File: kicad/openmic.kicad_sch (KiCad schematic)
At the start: 0 parts

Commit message: #13
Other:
- sheet codec ports: added CCLK; removed none
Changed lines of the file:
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@@
+	(wire
+		(pts
+			(xy 157.48 132.08) (xy 146.05 132.08)
+		)
+		(stroke
+			(width 0)
+			(type default)
+		)
+	)
 	(wire
 		(pts
@@
 	(wire
 		(pts
-			(xy 161.29 95.25) (xy 161.29 132.08)
-		)
-		(stroke
-			(width 0)
-			(type default)
-		)
-	)
-	(wire
-		(pts
-			(xy 146.05 132.08) (xy 161.29 132.08)
+			(xy 161.29 95.25) (xy 161.29 135.89)
+		)
+		(stroke
+			(width 0)
+			(type default)
+		)
+	)
+	(wire
+		(pts
+			(xy 146.05 135.89) (xy 161.29 135.89)
 		)
 		(stroke
@@
 	(wire
 		(pts
+			(xy 157.48 99.06) (xy 157.48 132.08)
+		)
+		(stroke
+			(width 0)
+			(type default)
+		)
+	)
+	(wire
+		(pts
 			(xy 101.6 139.7) (xy 101.6 91.44)
 		)
@@
 	(wire
 		(pts
+			(xy 146.05 99.06) (xy 157.48 99.06)
+		)
+		(stroke
+			(width 0)
+			(type default)
+		)
+	)
+	(wire
+		(pts
 			(xy 146.05 106.68) (xy 149.86 106.68)
 		)
@@
 	(wire
 		(pts
-			(xy 165.1 91.44) (xy 165.1 135.89)
+			(xy 165.1 91.44) (xy 165.1 139.7)
 		)
 		(stroke
@@
 	(wire
 		(pts
-			(xy 146.05 135.89) (xy 165.1 135.89)
+			(xy 146.05 139.7) (xy 165.1 139.7)
 		)
 		(stroke
@@
 		)
 		(pin "DIN" input
+			(at 146.05 139.7 0)
+			(effects
+				(font
+					(size 1.27 1.27)
+				)
+				(justify right)
+			)
+		)
+		(pin "DOUT" output
 			(at 146.05 135.89 0)
-			(effects
-				(font
-					(size 1.27 1.27)
-				)
-				(justify right)
-			)
-		)
-		(pin "DOUT" output
-			(at 146.05 132.08 0)
 			(effects
 				(font
@@
 			(effects
 				(font
+					(size 1.27 1.27)
+				)
+				(justify right)
+			)
+		)
+		(pin "CCLK" input
+			(at 146.05 132.08 0)
+			(effects
+				(font

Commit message: #14
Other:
- sheet input ports: added LED_1_DIN, LED_1_DOUT, LED_2_DIN, LED_2_DOUT; removed none
- sheet usb bridge ports: added LED_CONTROL; removed none
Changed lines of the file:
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@@
+	(wire
+		(pts
+			(xy 53.34 48.26) (xy 120.65 48.26)
+		)
+		(stroke
+			(width 0)
+			(type default)
+		)
+	)
 	(wire
 		(pts
@@
 	(wire
 		(pts
+			(xy 57.15 57.15) (xy 53.34 57.15)
+		)
+		(stroke
+			(width 0)
+			(type default)
+		)
+	)
+	(wire
+		(pts
 			(xy 120.65 132.08) (xy 109.22 132.08)
 		)
@@
 	(wire
 		(pts
-			(xy 53.34 30.48) (xy 53.34 54.61)
+			(xy 49.53 38.1) (xy 49.53 80.01)
 		)
 		(stroke
@@
 	(wire
 		(pts
-			(xy 53.34 30.48) (xy 57.15 30.48)
+			(xy 49.53 38.1) (xy 57.15 38.1)
 		)
 		(stroke
@@
 	(wire
 		(pts
+			(xy 53.34 64.77) (xy 57.15 64.77)
+		)
+		(stroke
+			(width 0)
+			(type default)
+		)
+	)
+	(wire
+		(pts
 			(xy 113.03 87.63) (xy 120.65 87.63)
 		)
@@
 	(wire
 		(pts
+			(xy 53.34 48.26) (xy 53.34 57.15)
+		)
+		(stroke
+			(width 0)
+			(type default)
+		)
+	)
+	(wire
+		(pts
 			(xy 153.67 128.27) (xy 153.67 102.87)
 		)
@@
 	(wire
 		(pts
-			(xy 57.15 54.61) (xy 53.34 54.61)
+			(xy 57.15 80.01) (xy 49.53 80.01)
 		)
 		(stroke
@@
 	(wire
 		(pts
+			(xy 57.15 60.96) (xy 53.34 60.96)
+		)
+		(stroke
+			(width 0)
+			(type default)
+		)
+	)
+	(wire
+		(pts
 			(xy 82.55 95.25) (xy 97.79 95.25)
+		)
+		(stroke
+			(width 0)
+			(type default)
+		)
+	)
+	(wire
+		(pts
+			(xy 53.34 60.96) (xy 53.34 64.77)
 		)
 		(stroke
@@
 		)
 		(pin "+48V_PH" input
-			(at 57.15 54.61 180)
+			(at 57.15 80.01 180)
 			(effects
 				(font
@@
 		)
 		(pin "BSY_1" output
-			(at 57.15 59.69 180)
+			(at 57.15 72.39 180)
 			(effects
 				(font
@@
 		)
 		(pin "BSY_2" output
-			(at 57.15 63.5 180)
+			(at 57.15 76.2 180)
 			(effects
 				(font
@@
 				)
 				(justify right)
+			)
+		)
+		(pin "LED_1_DIN" input
+			(at 57.15 57.15 180)
+			(effects
+				(font
+					(size 1.27 1.27)
+				)
+				(justify left)
+			)
+		)
+		(pin "LED_1_DOUT" output
+			(at 57.15 60.96 180)
+			(effects
+				(font
+					(size 1.27 1.27)
+				)
+				(justify left)
+			)
+		)
+		(pin "LED_2_DIN" input
+			(at 57.15 64.77 180)
+			(effects
+				(font
+					(size 1.27 1.27)
+				)
+				(justify left)
+			)
+		)
+		(pin "LED_2_DOUT" output
+			(at 57.15 68.58 180)
+			(effects
+				(font
+					(size 1.27 1.27)
+				)
+				(justify left)
 			)
 		)
@@
 		)
 		(pin "+48V_PH" output
-			(at 57.15 30.48 180)
+			(at 57.15 38.1 180)
 			(effects
 				(font
@@
 			(effects
 				(font
+					(size 1.27 1.27)
+				)
+				(justify left)
+			)
+		)
+		(pin "LED_CONTROL" output
+			(at 120.65 48.26 180)
+			(effects
+				(font

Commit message: phones out
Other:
- added sheet monitor (monitor.kicad_sch)
- sheet heaphone driver ports: added LED_DIN, LED_DOUT, PHONES_EN, PHONES_IND, ROT_A, ROT_B; removed none
- sheet line driver ports: added none; removed IN_L, IN_R
- sheet usb bridge ports: added LINE_IND_L, LINE_IND_R, PHONES_EN, PHONES_IND; removed GPO_3, IND_1, IND_2, IND_3

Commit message: line out
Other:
- sheet usb bridge ports: added none; removed GPO_4

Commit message: input enable
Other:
- sheet input ports: added IN_EN_1, IN_EN_2; removed none

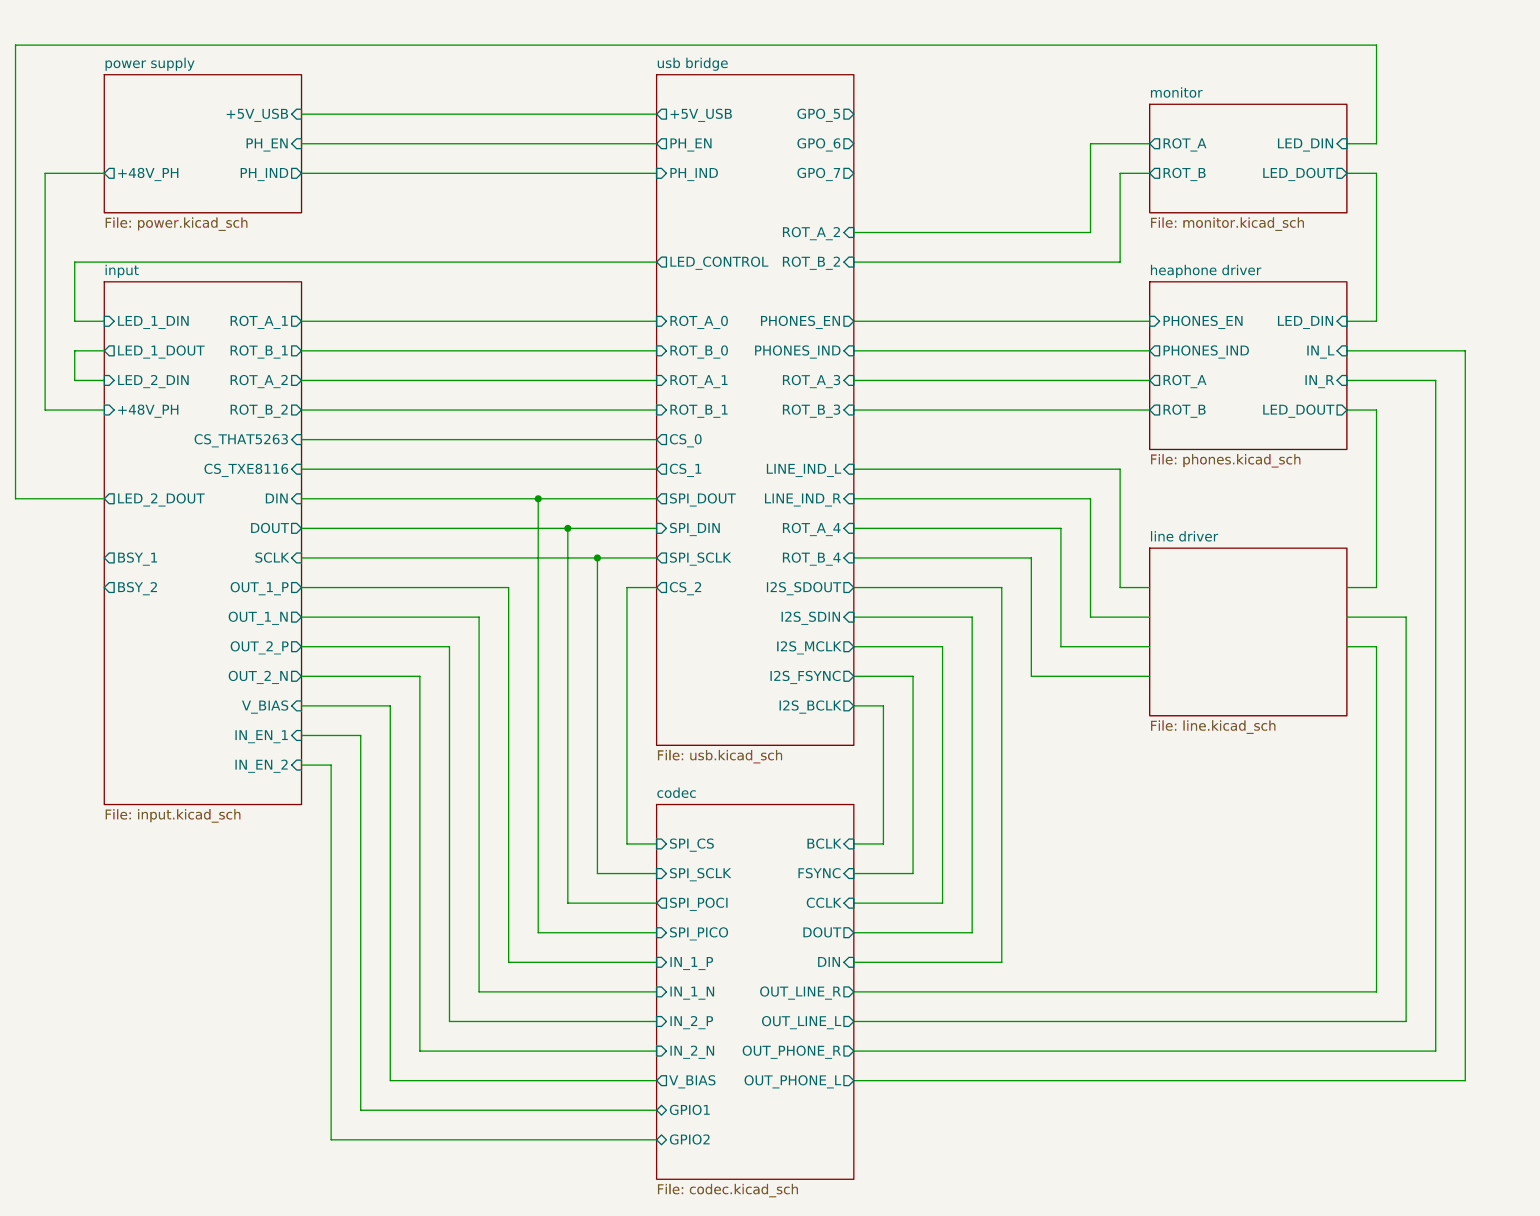
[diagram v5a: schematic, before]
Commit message: monitor switch
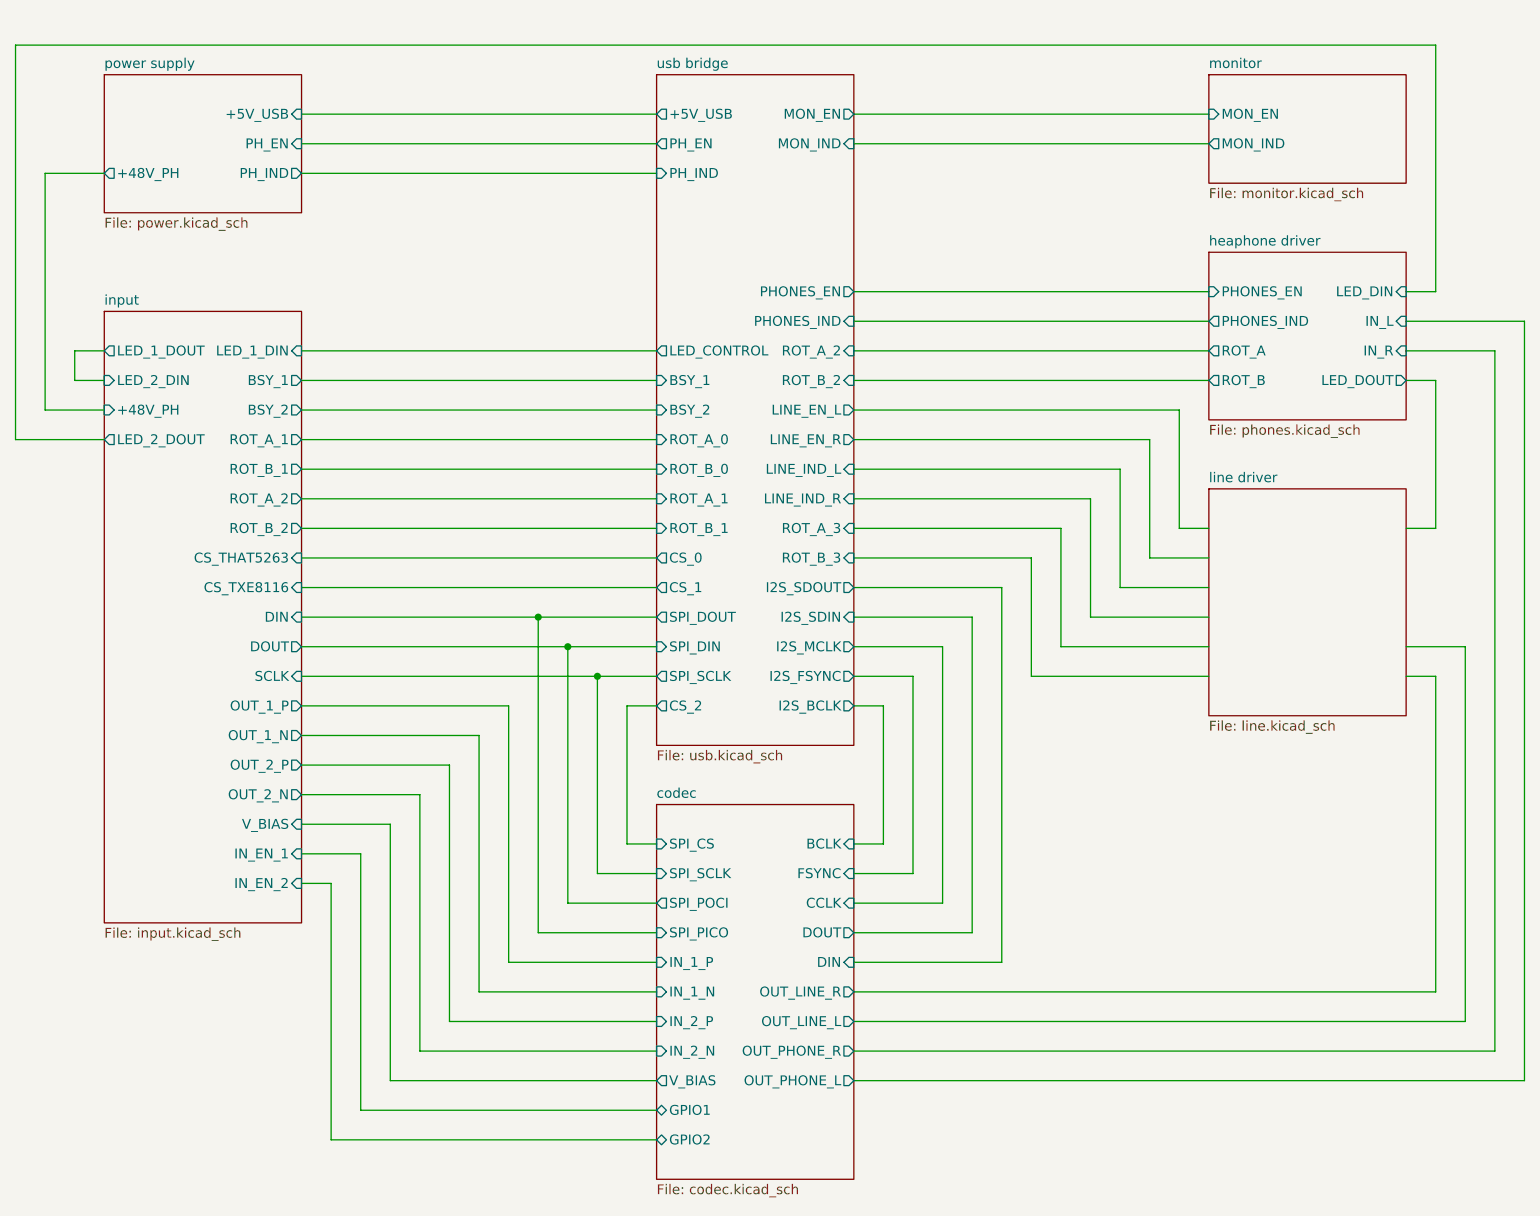
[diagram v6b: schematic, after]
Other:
- sheet monitor ports: added MON_EN, MON_IND; removed LED_DIN, LED_DOUT, ROT_A, ROT_B
- sheet usb bridge ports: added BSY_1, BSY_2, LINE_EN_L, LINE_EN_R, MON_EN, MON_IND; removed GPO_5, GPO_6, GPO_7, ROT_A_4, ROT_B_4

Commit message: line out
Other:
- sheet line driver ports: added IN_L, IN_R, LED_DIN, LED_DOUT, LINE_EN_L, LINE_EN_R, LINE_IND_L, LINE_IND_R, ROT_A, ROT_B; removed none
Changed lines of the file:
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@@
+			)
+		)
+		(pin "IN_L" input
+			(at 217.17 99.06 0)
+			(effects
+				(font
+					(size 1.27 1.27)
+				)
+				(justify right)
+			)
+		)
+		(pin "IN_R" input
+			(at 217.17 102.87 0)
+			(effects
+				(font
+					(size 1.27 1.27)
+				)
+				(justify right)
+			)
+		)
+		(pin "LED_DIN" input
+			(at 217.17 83.82 0)
+			(effects
+				(font
+					(size 1.27 1.27)
+				)
+				(justify right)
+			)
+		)
+		(pin "LED_DOUT" output
+			(at 217.17 87.63 0)
+			(effects
+				(font
+					(size 1.27 1.27)
+				)
+				(justify right)
+			)
+		)
+		(pin "LINE_EN_L" input
+			(at 191.77 83.82 180)
+			(effects
+				(font
+					(size 1.27 1.27)
+				)
+				(justify left)
+			)
+		)
+		(pin "LINE_EN_R" input
+			(at 191.77 87.63 180)
+			(effects
+				(font
+					(size 1.27 1.27)
+				)
+				(justify left)
+			)
+		)
+		(pin "LINE_IND_L" output
+			(at 191.77 91.44 180)
+			(effects
+				(font
+					(size 1.27 1.27)
+				)
+				(justify left)
+			)
+		)
+		(pin "LINE_IND_R" output
+			(at 191.77 95.25 180)
+			(effects
+				(font
+					(size 1.27 1.27)
+				)
+				(justify left)
+			)
+		)
+		(pin "ROT_A" output
+			(at 191.77 99.06 180)
+			(effects
+				(font
+					(size 1.27 1.27)
+				)
+				(justify left)
+			)
+		)
+		(pin "ROT_B" output
+			(at 191.77 102.87 180)
+			(effects
+				(font
+					(size 1.27 1.27)
+				)
+				(justify left)
 			)
 		)

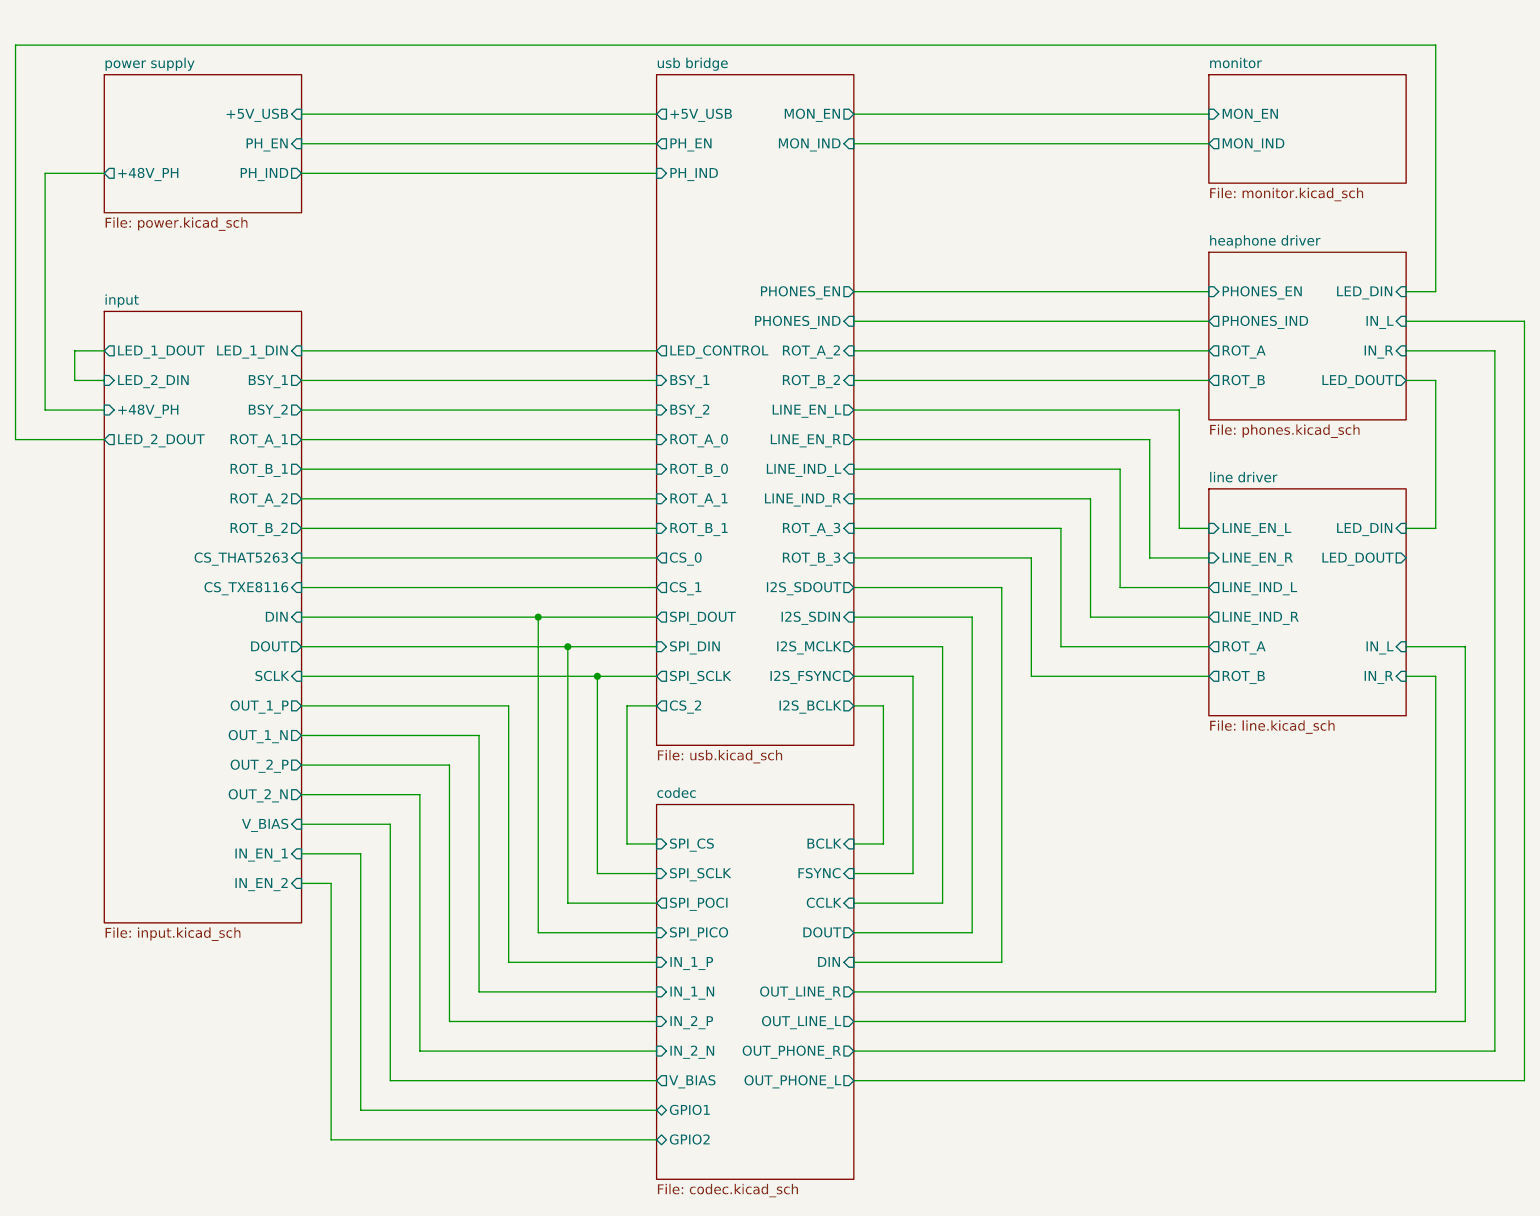
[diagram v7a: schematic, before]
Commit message: external power supply (#9)
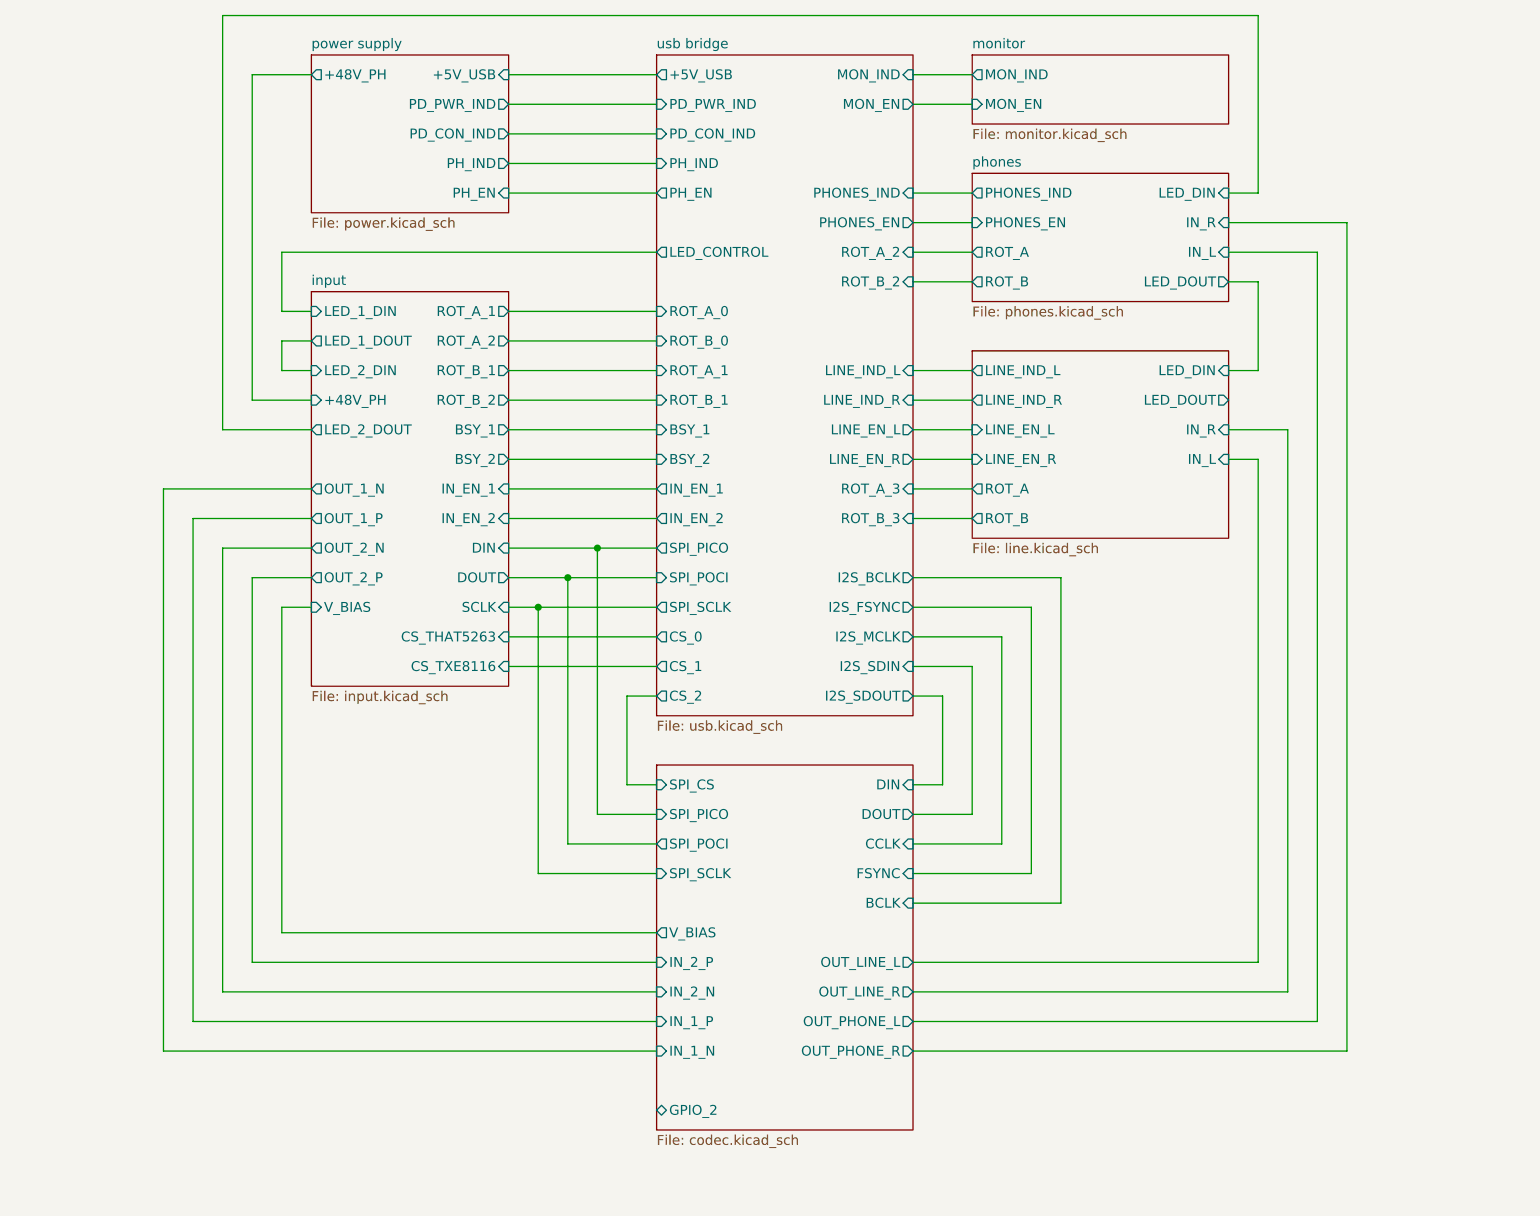
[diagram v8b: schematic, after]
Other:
- removed sheet heaphone driver
- added sheet phones (phones.kicad_sch)
- sheet codec ports: added GPIO_2; removed GPIO1, GPIO2
- sheet power supply ports: added PD_CON_IND, PD_PWR_IND; removed none
- sheet usb bridge ports: added IN_EN_1, IN_EN_2, PD_CON_IND, PD_PWR_IND, SPI_PICO, SPI_POCI; removed SPI_DIN, SPI_DOUT
